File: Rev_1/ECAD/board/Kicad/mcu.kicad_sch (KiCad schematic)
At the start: 1 part

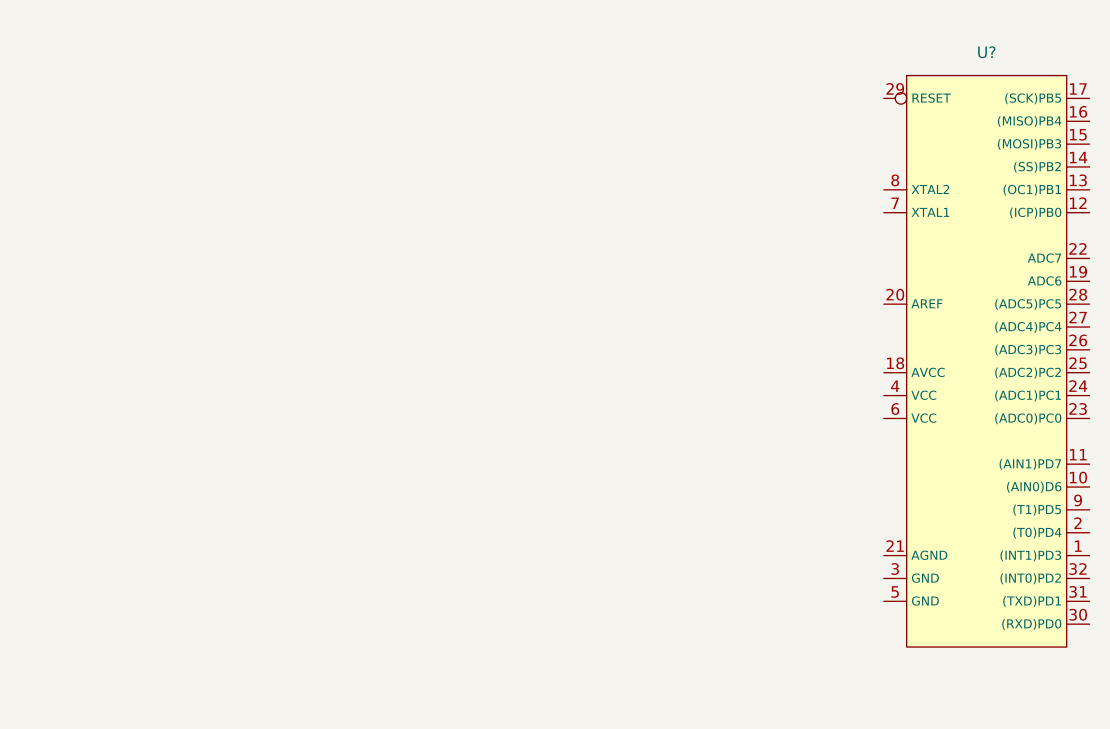
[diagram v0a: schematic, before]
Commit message: Added MCU sketch
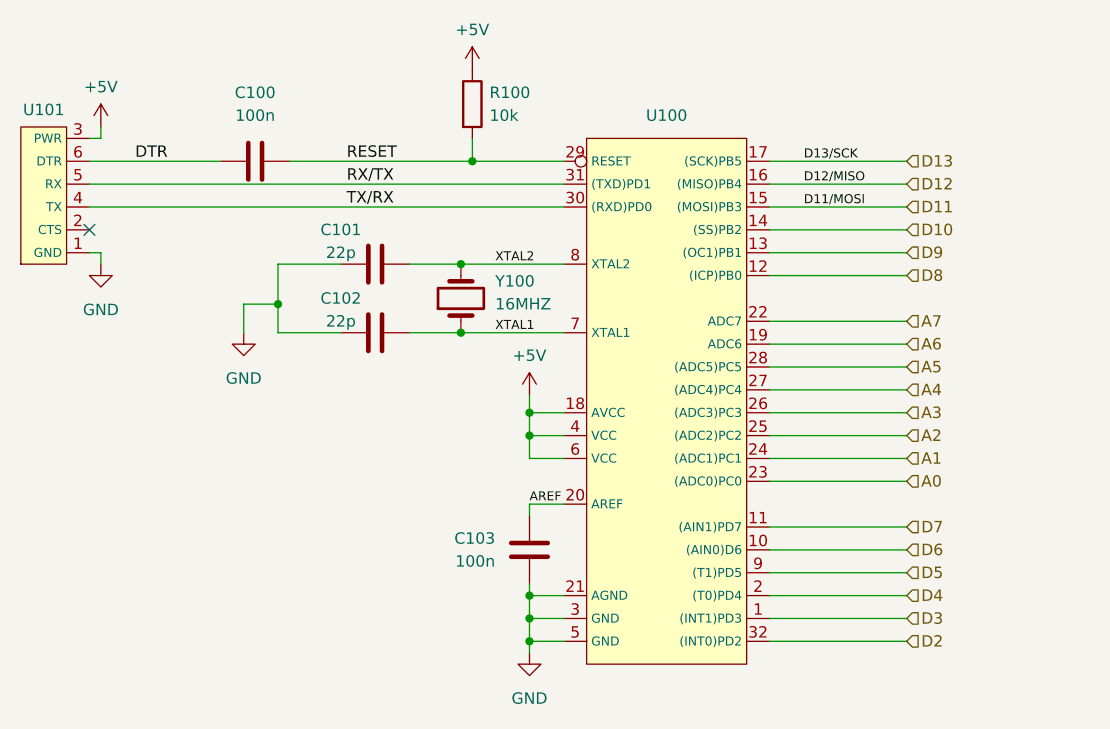
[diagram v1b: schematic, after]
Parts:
- added C100, C103: 100n, Capacitor_SMD:C_0805_2012Metric_Pad1.18x1.45mm_HandSolder, symbol Device:C
- added C101, C102: 22p, Capacitor_SMD:C_0805_2012Metric_Pad1.18x1.45mm_HandSolder, symbol Device:C
- added R100: 10k, Resistor_SMD:R_0805_2012Metric_Pad1.20x1.40mm_HandSolder, symbol Device:R
- added U101: ~, symbol EEPROM_PROGRAMMER:FT232RL
- added Y100: 16MHZ, symbol Device:Crystal
- gave numbers to parts that had none: 1
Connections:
- net D3: now reaches U100.1 ((INT1)PD3)
- net D6: now reaches U100.10 ((AIN0)D6)
- net D7: now reaches U100.11 ((AIN1)PD7)
- net D8: now reaches U100.12 ((ICP)PB0)
- net D9: now reaches U100.13 ((OC1)PB1)
- net D10: now reaches U100.14 ((SS)PB2)
- net D11: now reaches U100.15 ((MOSI)PB3)
- net D12: now reaches U100.16 ((MISO)PB4)
- net D13: now reaches U100.17 ((SCK)PB5)
- net +5V: now reaches U100.18 (AVCC)
- net +5V: now also U100.4 (VCC), U100.6 (VCC), R100.1, U101.3 (PWR)
- net A6: now reaches U100.19 (ADC6)
- net D4: now reaches U100.2 ((T0)PD4)
- net AREF: now reaches U100.20 (AREF)
- net AREF: now also C103.1
- net GND: now reaches U100.21 (AGND)
- net GND: now also U100.3 (GND), U100.5 (GND), C101.1, C102.1, C103.2, U101.1 (GND)
- net A7: now reaches U100.22 (ADC7)
- net A0: now reaches U100.23 ((ADC0)PC0)
- net A1: now reaches U100.24 ((ADC1)PC1)
- net A2: now reaches U100.25 ((ADC2)PC2)
- net A3: now reaches U100.26 ((ADC3)PC3)
- net A4: now reaches U100.27 ((ADC4)PC4)
- net A5: now reaches U100.28 ((ADC5)PC5)
- net RESET: now reaches U100.29 (RESET)
- net RESET: now also C100.2, R100.2
- net TX/RX: now reaches U100.30 ((RXD)PD0)
- net TX/RX: now also U101.4 (TX)
- net RX/TX: now reaches U100.31 ((TXD)PD1)
- net RX/TX: now also U101.5 (RX)
- net D2: now reaches U100.32 ((INT0)PD2)
- net XTAL1: now reaches U100.7 (XTAL1)
- net XTAL1: now also C102.2, Y100.1
- net XTAL2: now reaches U100.8 (XTAL2)
- net XTAL2: now also C101.2, Y100.2
- net D5: now reaches U100.9 ((T1)PD5)
- new net DTR: C100.1, U101.6 (DTR)
- no-connect marks 0 -> 1
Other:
- moved on the sheet: U100

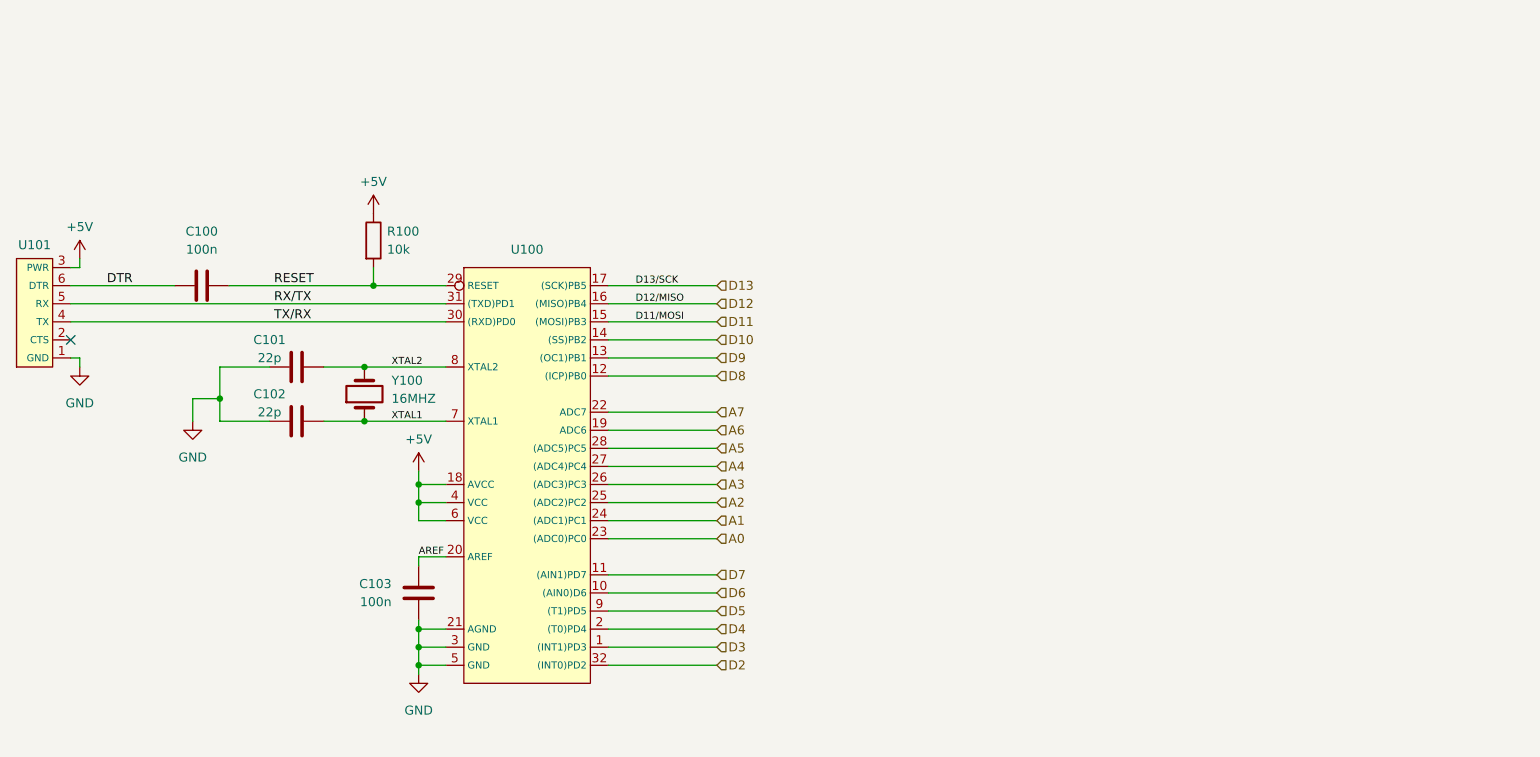
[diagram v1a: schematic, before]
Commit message: Added USB Power circiut
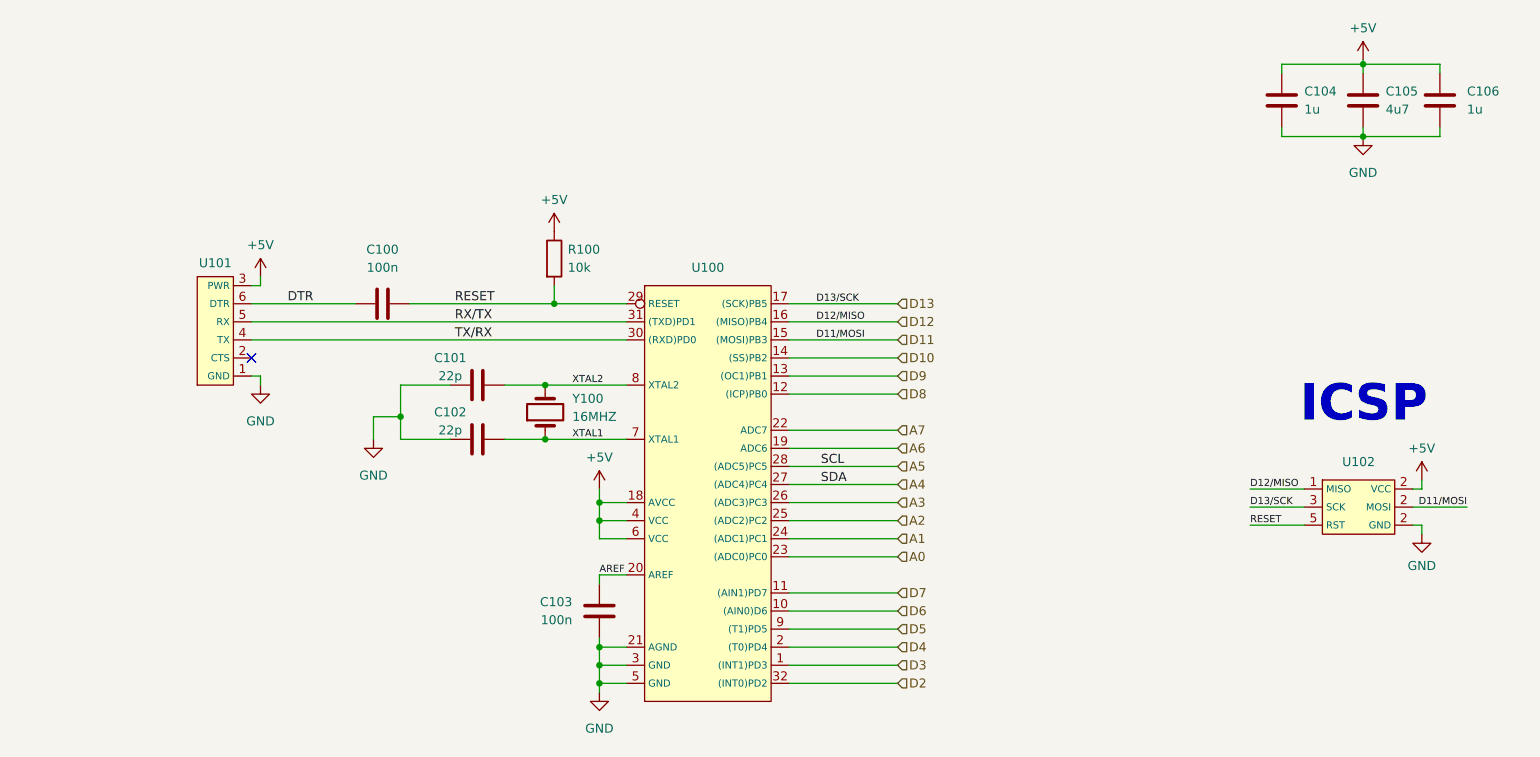
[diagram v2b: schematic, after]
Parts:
- added C104, C106: 1u, Capacitor_SMD:C_0805_2012Metric_Pad1.18x1.45mm_HandSolder, symbol Device:C
- added C105: 4u7, Capacitor_SMD:C_0805_2012Metric_Pad1.18x1.45mm_HandSolder, symbol Device:C
- added U102: ~, symbol EEPROM_PROGRAMMER:ICSP
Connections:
- net +5V: now also C104.2, C105.2, C106.2, U102.2 (VCC)
- net D11: now also U102.2 (VCC)
- net D12: now also U102.1 (MISO)
- net D13: now also U102.3 (SCK)
- net GND: now also C104.1, C105.1, C106.1, U102.2 (VCC)
- net RESET: now also U102.5 (RST)
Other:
- note added: "ICSP"
- moved on the sheet: C100, C101, C102, C103, R100, U100, U101, Y100

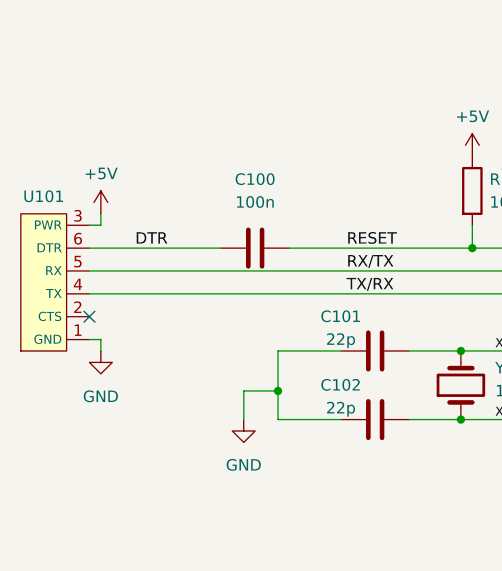
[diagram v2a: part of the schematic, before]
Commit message: Added power unit, and started on the logic block
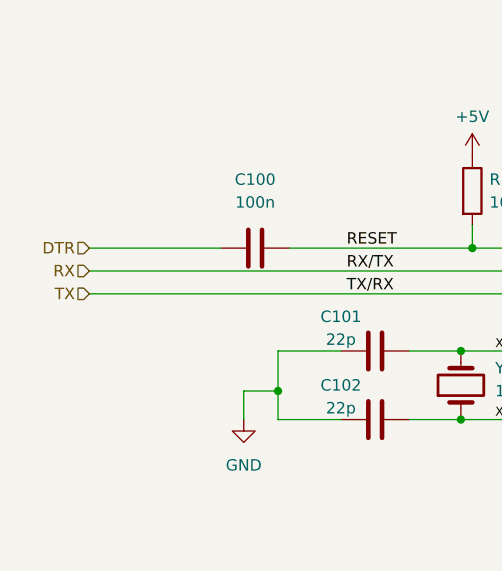
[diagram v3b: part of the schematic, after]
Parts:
- removed U101: ~, symbol EEPROM_PROGRAMMER:FT232RL
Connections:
- net RX/TX renamed RX
- net TX/RX renamed TX
- no-connect marks 1 -> 0
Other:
- title: (none) -> EEPROM Programer
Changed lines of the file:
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@@
 (kicad_sch (version 20230121) (generator eeschema)
   (paper "A4")
+  (title_block
+    (title "EEPROM Programer")
+    (date "2024-06-21")
+    (rev "1")
+  )
   (junction (at 120.65 93.345) (diameter 0) (color 0 0 0 0)
   )
@@
   (junction (at 128.27 102.235) (diameter 0) (color 0 0 0 0)
   )
-  (no_connect (at 79.375 81.915))
   (wire (pts (xy 128.27 127.635) (xy 128.27 128.905))
     (stroke (width 0) (type default))
@@
     (stroke (width 0) (type default))
   )
-  (wire (pts (xy 80.645 70.485) (xy 80.645 71.755))
-    (stroke (width 0) (type default))
-  )
   (wire (pts (xy 114.935 85.725) (xy 120.65 85.725))
     (stroke (width 0) (type default))
   )
-  (wire (pts (xy 79.375 84.455) (xy 80.645 84.455))
-    (stroke (width 0) (type default))
-  )
   (wire (pts (xy 79.375 74.295) (xy 93.98 74.295))
     (stroke (width 0) (type default))
@@
     (stroke (width 0) (type default))
   )
-  (wire (pts (xy 79.375 71.755) (xy 80.645 71.755))
-    (stroke (width 0) (type default))
-  )
   (wire (pts (xy 128.27 125.095) (xy 128.27 127.635))
     (stroke (width 0) (type default))
@@
   )
   (wire (pts (xy 96.52 90.17) (xy 96.52 93.345))
-    (stroke (width 0) (type default))
-  )
-  (wire (pts (xy 80.645 84.455) (xy 80.645 85.725))
     (stroke (width 0) (type default))
   )
@@
     (effects (font (size 1.27 1.27)) (justify left bottom))
   )
-  (label "DTR" (at 84.455 74.295 0) (fields_autoplaced)
-    (effects (font (size 1.27 1.27)) (justify left bottom))
-  )
   (label "RESET" (at 219.71 105.41 0) (fields_autoplaced)
     (effects (font (size 1 1)) (justify left bottom))
@@
     (effects (font (size 1.27 1.27)) (justify left))
   )
+  (hierarchical_label "RX" (shape input) (at 79.375 76.835 180) (fields_autoplaced)
+    (effects (font (size 1.27 1.27)) (justify right))
+  )
+  (hierarchical_label "DTR" (shape input) (at 79.375 74.295 180) (fields_autoplaced)
+    (effects (font (size 1.27 1.27)) (justify right))
+  )
   (hierarchical_label "D13" (shape input) (at 170.18 74.295 0) (fields_autoplaced)
     (effects (font (size 1.27 1.27)) (justify left))
@@
   (hierarchical_label "A7" (shape input) (at 170.18 92.075 0) (fields_autoplaced)
     (effects (font (size 1.27 1.27)) (justify left))
+  )
+  (hierarchical_label "TX" (shape input) (at 79.375 79.375 180) (fields_autoplaced)
+    (effects (font (size 1.27 1.27)) (justify right))
   )
   (hierarchical_label "D12" (shape input) (at 170.18 76.835 0) (fields_autoplaced)
@@
     )
   )
-  (symbol (lib_id "power:GND") (at 80.645 85.725 0) (unit 1)
-    (in_bom yes) (on_board yes) (dnp no) (fields_autoplaced)
-    (property "Reference" "#PWR04" (at 80.645 92.075 0)
-      (effects (font (size 1.27 1.27)) hide)
-    )
-    (property "Value" "GND" (at 80.645 90.805 0)
-      (effects (font (size 1.27 1.27)))
-    )
-    (property "Footprint" "" (at 80.645 85.725 0)
-      (effects (font (size 1.27 1.27)) hide)
-    )
-    (property "Datasheet" "" (at 80.645 85.725 0)
-      (effects (font (size 1.27 1.27)) hide)
-    )
-    (pin "1")
-    (instances
-      (project "board"
-        (path "/2f4d49fd-9c63-4eb5-a266-4b5553b3e489/a9c4ef02-6c48-4ddc-bd95-3bc4e5cf2494"
-          (reference "#PWR04") (unit 1)
-        )
-      )
-    )
-  )
   (symbol (lib_id "Device:C") (at 97.79 74.295 90) (unit 1)
     (in_bom yes) (on_board yes) (dnp no) (fields_autoplaced)
@@
         (path "/2f4d49fd-9c63-4eb5-a266-4b5553b3e489/a9c4ef02-6c48-4ddc-bd95-3bc4e5cf2494"
           (reference "C106") (unit 1)
-        )
-      )
-    )
-  )
-  (symbol (lib_id "EEPROM_PROGRAMMER:FT232RL") (at 74.295 78.105 90) (unit 1)
-    (in_bom yes) (on_board yes) (dnp no) (fields_autoplaced)
-    (property "Reference" "U101" (at 74.295 68.58 90)
-      (effects (font (size 1.27 1.27)))
-    )
-    (property "Value" "~" (at 74.295 78.105 0)
-      (effects (font (size 1.27 1.27)))
-    )
-    (property "Footprint" "" (at 74.295 78.105 0)
-      (effects (font (size 1.27 1.27)) hide)
-    )
-    (property "Datasheet" "https://www.electrokit.com/upload/product/12201/12201001/FTDI_Basic-v21-5V.pdf" (at 67.945 78.105 0)
-      (effects (font (size 1.27 1.27)) hide)
-    )
-    (pin "1")
-    (pin "2")
-    (pin "3")
-    (pin "4")
-    (pin "5")
-    (pin "6")
-    (instances
-      (project "board"
-        (path "/2f4d49fd-9c63-4eb5-a266-4b5553b3e489/a9c4ef02-6c48-4ddc-bd95-3bc4e5cf2494"
-          (reference "U101") (unit 1)
         )
       )
@@
         )
       )
-    )
-  )
-  (symbol (lib_id "power:+5V") (at 80.645 70.485 0) (unit 1)
-    (in_bom yes) (on_board yes) (dnp no) (fields_autoplaced)
-    (property "Reference" "#PWR01" (at 80.645 74.295 0)
-      (effects (font (size 1.27 1.27)) hide)
-    )
-    (property "Value" "+5V" (at 80.645 66.04 0)
-      (effects (font (size 1.27 1.27)))
-    )
-    (property "Footprint" "" (at 80.645 70.485 0)
-      (effects (font (size 1.27 1.27)) hide)
-    )
-    (property "Datasheet" "" (at 80.645 70.485 0)
-      (effects (font (size 1.27 1.27)) hide)
-    )
-    (pin "1")
-    (instances
-      (project "board"
-        (path "/2f4d49fd-9c63-4eb5-a266-4b5553b3e489/a9c4ef02-6c48-4ddc-bd95-3bc4e5cf2494"
-          (reference "#PWR01") (unit 1)
-        )
-      )
